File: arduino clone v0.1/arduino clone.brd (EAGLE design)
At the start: 68.6 x 26.2 mm, 47 parts, among them J203 ICSP HEADER, J402 FTDI Breakout Header, U101 ATMEGA328P_TQFP, U301 CH340G, Y101 16MHz, Y301 12MHz

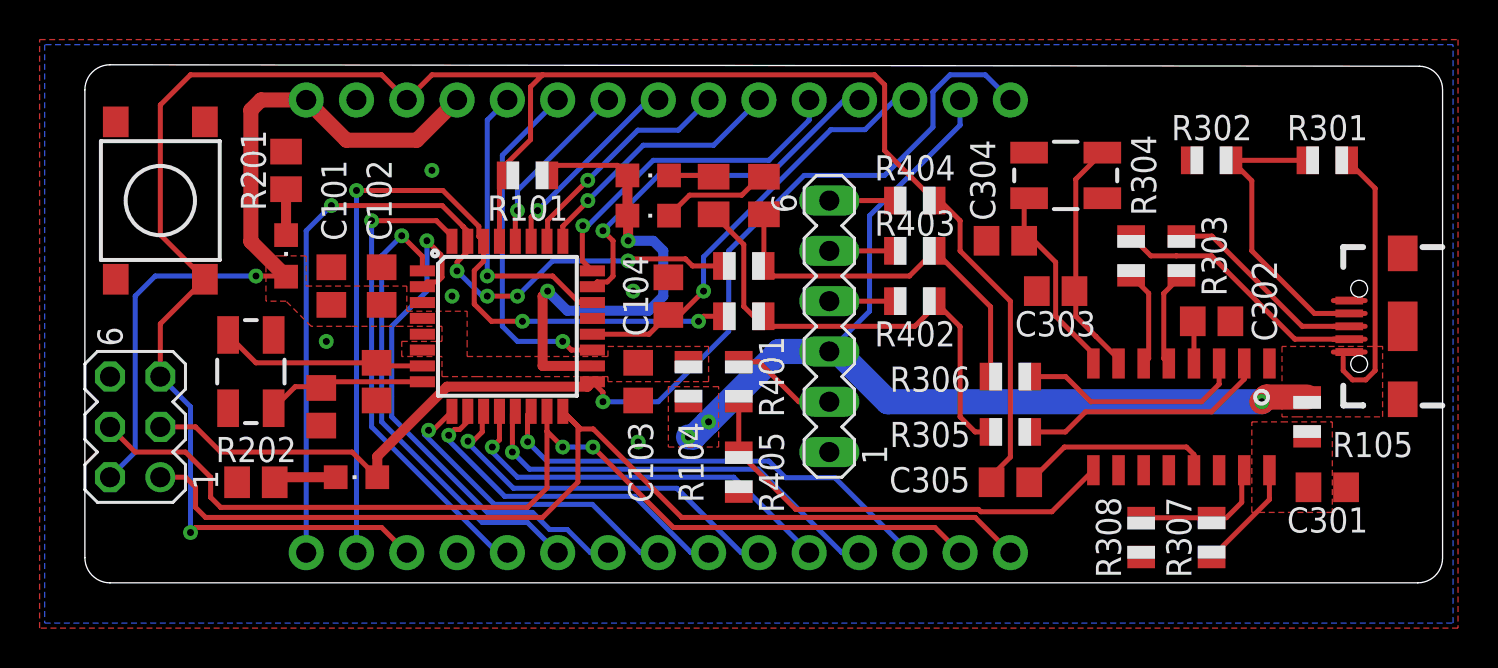
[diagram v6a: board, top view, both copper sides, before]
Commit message: remove wire stubs
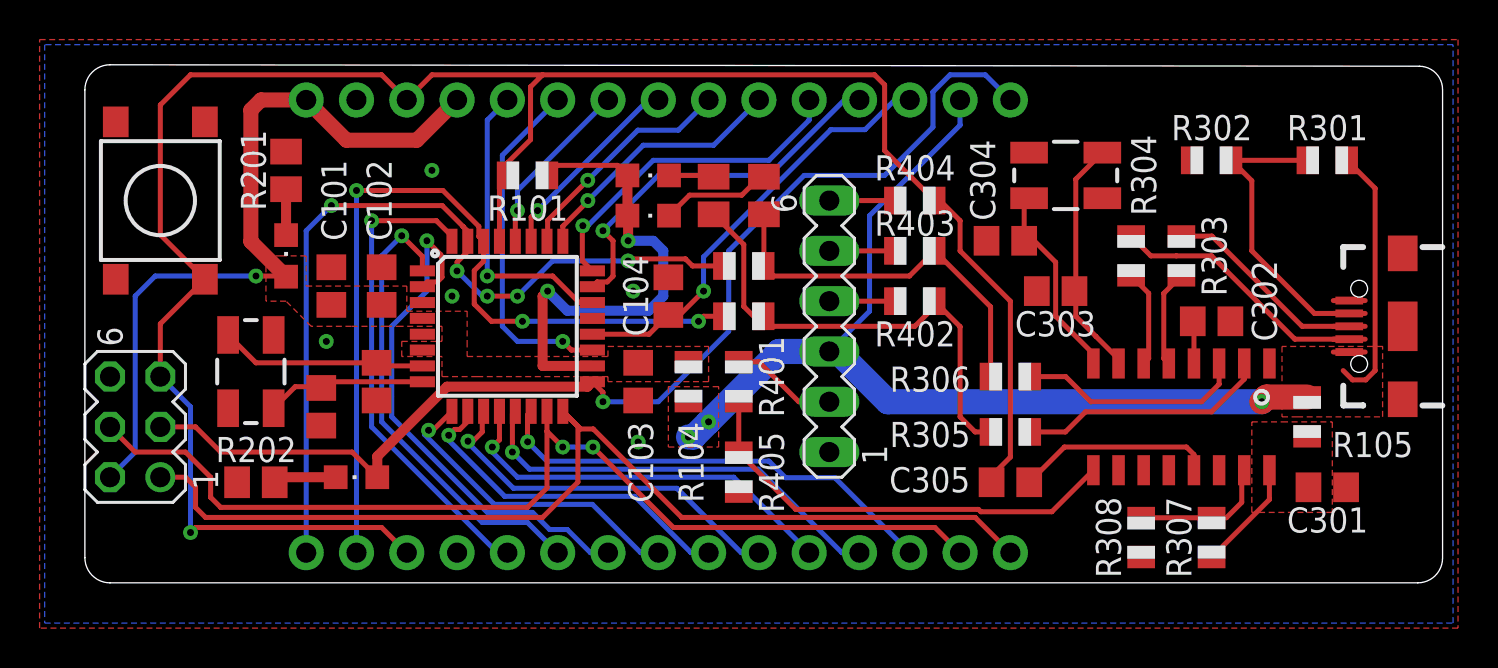
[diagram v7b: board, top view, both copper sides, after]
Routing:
- net PP5V0_USB: track 63.5 -> 62.8 mm
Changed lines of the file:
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@@
 <via x="40.894" y="46.228" extent="1-16" drill="0.35"/>
 <via x="40.64" y="53.848" extent="1-16" drill="0.35"/>
-<wire x1="72.771" y1="50.193" x2="76.802" y2="53.37" width="0" layer="19" extent="1-1"/>
-<wire x1="70.8" y1="52.324" x2="72.771" y2="50.193" width="0" layer="19" extent="1-1"/>
-<wire x1="76.642" y1="43.942" x2="72.771" y2="50.193" width="0" layer="19" extent="1-1"/>
-<wire x1="68.85" y1="60.452" x2="70.8" y2="52.324" width="0" layer="19" extent="1-1"/>
-<wire x1="61.026" y1="53.848" x2="70.8" y2="52.324" width="0" layer="19" extent="1-1"/>
-<wire x1="58.486" y1="56.388" x2="61.026" y2="53.848" width="0" layer="19" extent="1-1"/>
-<wire x1="66.294" y1="40.402" x2="76.642" y2="43.942" width="0" layer="19" extent="1-1"/>
-<wire x1="50.546" y1="45.72" x2="61.026" y2="53.848" width="0" layer="19" extent="1-1"/>
-<wire x1="45.974" y1="43.704" x2="50.546" y2="45.72" width="0" layer="19" extent="1-1"/>
-<wire x1="40.894" y1="46.228" x2="45.974" y2="43.704" width="0" layer="19" extent="1-1"/>
-<wire x1="40.894" y1="48.326" x2="40.894" y2="46.228" width="0" layer="19" extent="1-1"/>
-<wire x1="38.5826" y1="52.47" x2="40.894" y2="48.326" width="0" layer="19" extent="1-1"/>
-<wire x1="40.64" y1="53.848" x2="38.5826" y2="52.47" width="0" layer="19" extent="1-1"/>
-<wire x1="42.418" y1="54.544" x2="40.64" y2="53.848" width="0" layer="19" extent="1-1"/>
-<wire x1="31.496" y1="53.594" x2="38.5826" y2="52.47" width="0" layer="19" extent="1-1"/>
-<wire x1="29.9974" y1="53.27" x2="31.496" y2="53.594" width="0" layer="19" extent="1-1"/>
-<wire x1="29.9974" y1="51.67" x2="29.9974" y2="53.27" width="0" layer="19" extent="1-1"/>
-<wire x1="27.94" y1="55.052" x2="29.9974" y2="53.27" width="0" layer="19" extent="1-1"/>
-<wire x1="25.4" y1="55.052" x2="27.94" y2="55.052" width="0" layer="19" extent="1-1"/>
-<wire x1="25.146" y1="51.308" x2="25.4" y2="55.052" width="0" layer="19" extent="1-1"/>
-<wire x1="27.686" y1="48.326" x2="25.146" y2="51.308" width="0" layer="19" extent="1-1"/>
-<wire x1="24.892" y1="47.056" x2="27.686" y2="48.326" width="0" layer="19" extent="1-1"/>
-<wire x1="20.64" y1="44.196" x2="24.892" y2="47.056" width="0" layer="19" extent="1-1"/>
-<wire x1="30.48" y1="59.944" x2="27.94" y2="55.052" width="0" layer="19" extent="1-1"/>
-<wire x1="26.67" y1="63.5" x2="30.48" y2="59.944" width="0" layer="19" extent="1-1"/>
-<wire x1="23.114" y1="60.894" x2="26.67" y2="63.5" width="0" layer="19" extent="1-1"/>
-<wire x1="14.224" y1="49.53" x2="20.64" y2="44.196" width="0" layer="19" extent="1-1"/>
-<wire x1="14.514" y1="54.445" x2="14.224" y2="49.53" width="0" layer="19" extent="1-1"/>
-<wire x1="31.75" y1="40.64" x2="27.686" y2="48.326" width="0" layer="19" extent="1-1"/>
 </signal>
 <signal name="MCU_RESET">
@@
 <wire x1="27.94" y1="64.77" x2="18.288" y2="64.77" width="0.254" layer="1"/>
 <wire x1="16.764" y1="56.695" x2="16.764" y2="63.246" width="0.254" layer="1"/>
-<wire x1="16.764" y1="49.7327625" x2="16.764" y2="49.53" width="0.254" layer="1"/>
 <wire x1="19.014" y1="54.445" x2="16.764" y2="56.695" width="0.254" layer="1"/>
 <wire x1="29.21" y1="63.5" x2="30.48" y2="64.77" width="0.254" layer="1"/>
@@
 <wire x1="77.63585625" y1="49.364" x2="76.96814375" y2="49.364" width="0.254" layer="1"/>
 <wire x1="76.96814375" y1="49.364" x2="76.496" y2="49.83614375" width="0.254" layer="1"/>
-<wire x1="76.496" y1="49.83614375" x2="76.496" y2="50.50385625" width="0.254" layer="1"/>
 <wire x1="78.108" y1="59.036" x2="78.108" y2="49.83614375" width="0.254" layer="1"/>
 <wire x1="76.692" y1="60.452" x2="78.108" y2="59.036" width="0.254" layer="1"/>

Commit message: add more gnd vias to push gnd plane out
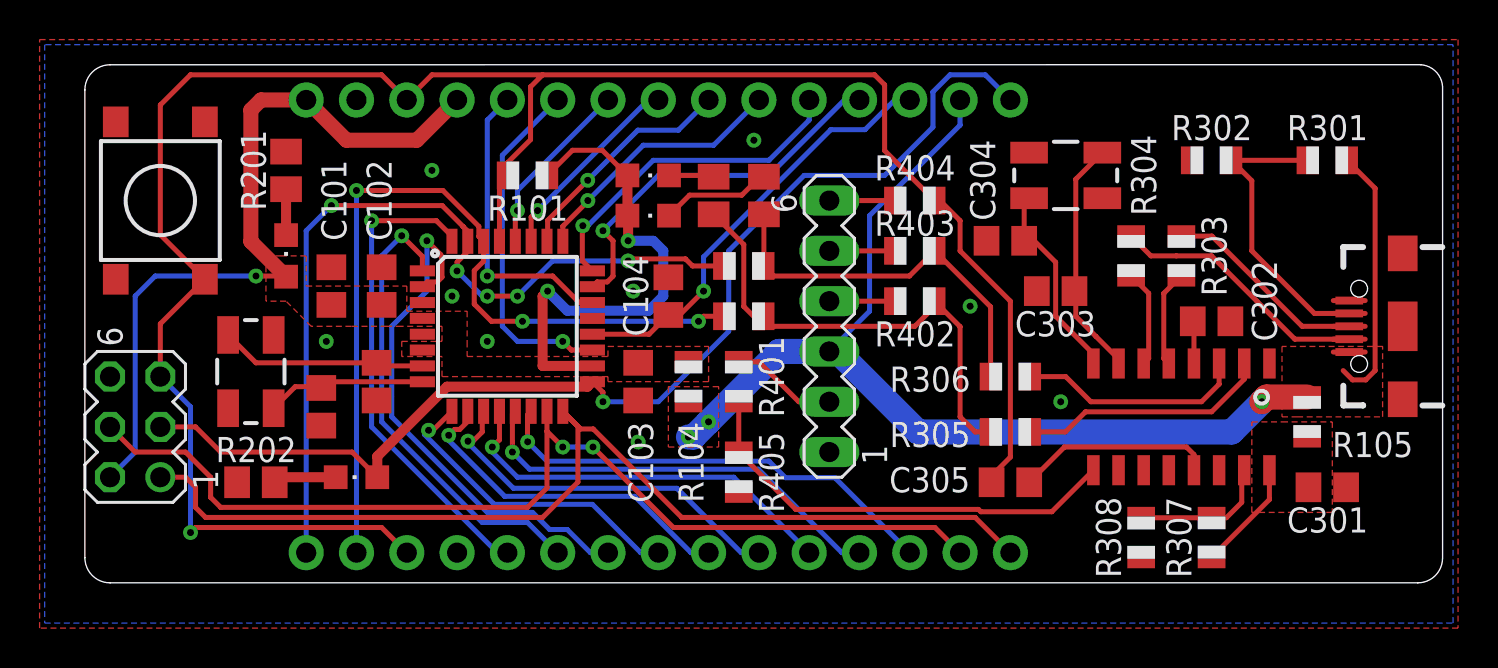
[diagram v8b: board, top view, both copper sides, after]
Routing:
- net PP5V0_USB: track 62.8 -> 64.1 mm
- net PP5V0_MCU: track 64.1 -> 64.8 mm
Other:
- outline, holes or cut-outs redrawn
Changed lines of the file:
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@@
 <wire x1="80.264" y1="39.116" x2="81.514" y2="40.366" width="0" layer="20" curve="90"/>
 <wire x1="81.514" y1="40.366" x2="81.514" y2="64.02745625" width="0" layer="20"/>
-<wire x1="81.514" y1="64.02745625" x2="80.33945625" y2="65.20330625" width="0" layer="20" curve="90"/>
-<wire x1="80.33945625" y1="65.20330625" x2="14.223353125" y2="65.276790625" width="0" layer="20"/>
+<wire x1="81.514" y1="64.02745625" x2="80.41565625" y2="65.27950625" width="0" layer="20" curve="90"/>
+<wire x1="80.41565625" y1="65.27950625" x2="14.223353125" y2="65.276790625" width="0" layer="20"/>
 <wire x1="14.223353125" y1="65.276790625" x2="12.954" y2="64.008846875" width="0" layer="20" curve="90"/>
 </plain>
@@
 <wire x1="16.51" y1="54.61" x2="21.59" y2="54.61" width="0.254" layer="16"/>
 <wire x1="40.352" y1="59.69" x2="40.352" y2="57.658" width="0.508" layer="1"/>
-<wire x1="36.814" y1="60.198" x2="39.844" y2="60.198" width="0.254" layer="1"/>
+<wire x1="37.576" y1="60.96" x2="39.082" y2="60.96" width="0.254" layer="1"/>
 <wire x1="40.352" y1="57.658" x2="40.386" y2="57.624" width="0.508" layer="1"/>
 <wire x1="40.386" y1="57.624" x2="40.386" y2="56.388" width="0.508" layer="1"/>
@@
 <wire x1="36.068" y1="53.594" x2="36.068" y2="50.07" width="0.508" layer="1"/>
 <wire x1="36.068" y1="50.07" x2="38.5826" y2="50.07" width="0.508" layer="1"/>
-<wire x1="36.306" y1="59.69" x2="36.814" y2="60.198" width="0.254" layer="1"/>
-<wire x1="39.844" y1="60.198" x2="40.352" y2="59.69" width="0.254" layer="1"/>
+<wire x1="36.306" y1="59.69" x2="37.576" y2="60.96" width="0.254" layer="1"/>
+<wire x1="39.082" y1="60.96" x2="40.352" y2="59.69" width="0.254" layer="1"/>
 <wire x1="36.322" y1="53.848" x2="36.068" y2="53.594" width="0.508" layer="1"/>
 <wire x1="42.164" y1="55.88" x2="42.164" y2="53.594" width="0.508" layer="16"/>
@@
 <via x="40.894" y="46.228" extent="1-16" drill="0.35"/>
 <via x="40.64" y="53.848" extent="1-16" drill="0.35"/>
+<via x="46.736" y="61.468" extent="1-16" drill="0.35"/>
+<via x="33.274" y="51.308" extent="1-16" drill="0.35"/>
+<via x="57.658" y="53.086" extent="1-16" drill="0.35"/>
+<via x="62.23" y="48.26" extent="1-16" drill="0.35"/>
 </signal>
 <signal name="MCU_RESET">
@@
 <wire x1="72.628" y1="48.498" x2="72.39" y2="48.26" width="1.27" layer="1"/>
 <via x="72.39" y="48.26" extent="1-16" drill="0.35"/>
-<wire x1="72.39" y1="48.26" x2="53.4991875" y2="48.26" width="1.27" layer="16"/>
-<wire x1="53.4991875" y1="48.26" x2="50.9591875" y2="50.8" width="1.27" layer="16"/>
+<wire x1="70.866" y1="46.736" x2="55.0231875" y2="46.736" width="1.27" layer="16"/>
+<wire x1="55.0231875" y1="46.736" x2="50.9591875" y2="50.8" width="1.27" layer="16"/>
 <wire x1="50.9591875" y1="50.8" x2="50.546" y2="50.8" width="1.27" layer="16"/>
 <wire x1="50.546" y1="50.8" x2="52.578" y2="52.832" width="0.254" layer="16"/>
@@
 <vertex x="44.958" y="49.022"/>
 </polygon>
+<wire x1="72.39" y1="48.26" x2="70.866" y2="46.736" width="1.27" layer="16"/>
 </signal>
 <signal name="PP5V0_CH340G">
